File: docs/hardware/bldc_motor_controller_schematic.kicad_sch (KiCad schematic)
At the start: 17 parts, among them J1 J_NUCLEO_I2C, J10 J_DRV8313_CTRL, J11 J_AS5600, J12 J_INA226, J13 J_SSD1306, J14 J_BARREL_JACK1, J2 J_NUCLEO_PWM, J3 J_NUCLEO_GPIO, J4 J_NUCLEO_UART, J5 J_NUCLEO_PWR, J7 J_MOTOR, J8 J_HM10, J9 J_DRV8313_OUT

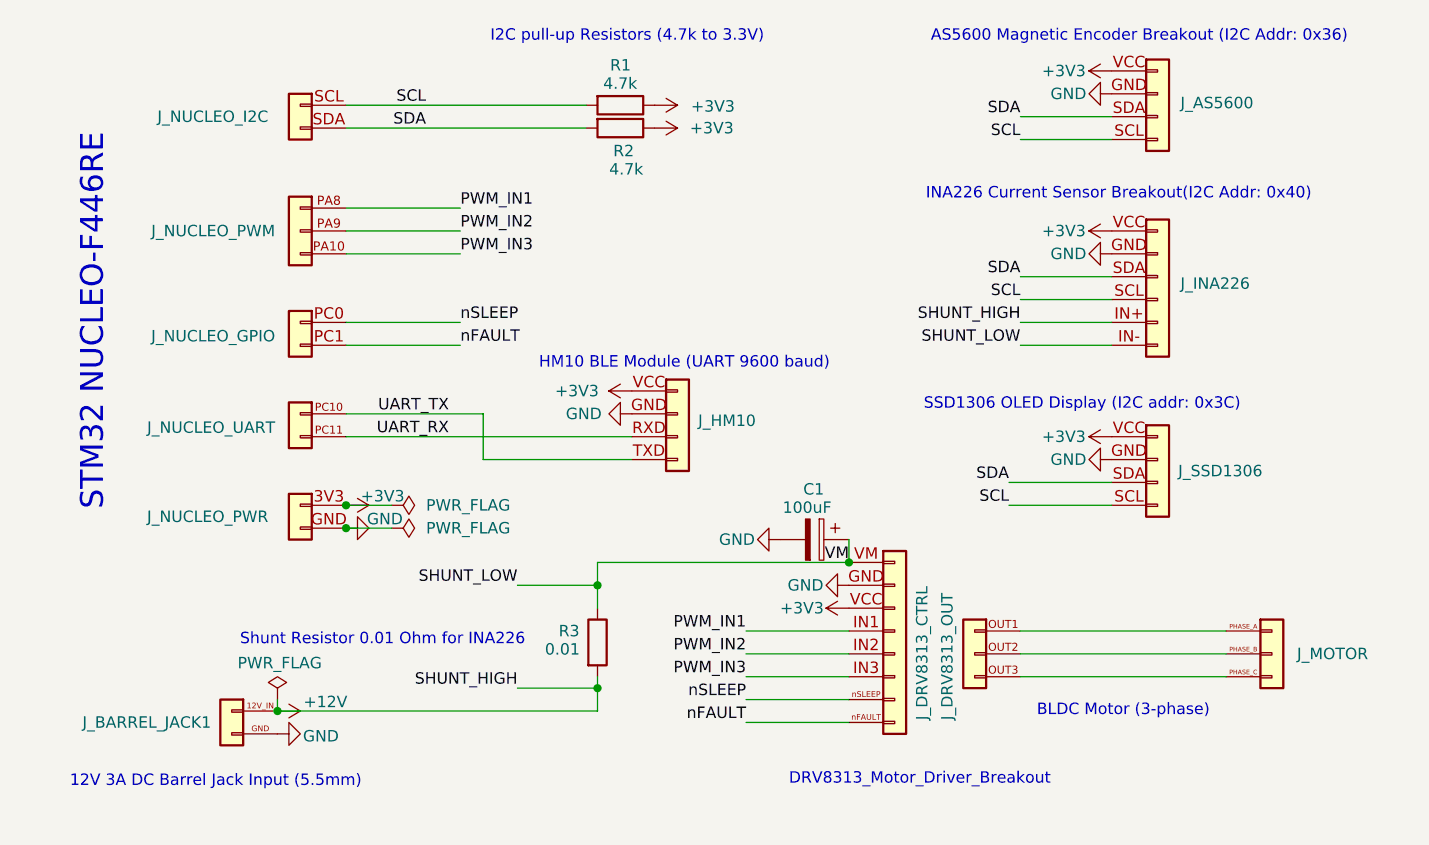
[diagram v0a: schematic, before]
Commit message: hw: update KiCad schematic files
- Remove on-board capacitor, pull-up resistors, and shunt resistor

- Add necessary pins to DRV8313 and INA226

- Fix UART to HM10 connections

- Add additional connections via net labels
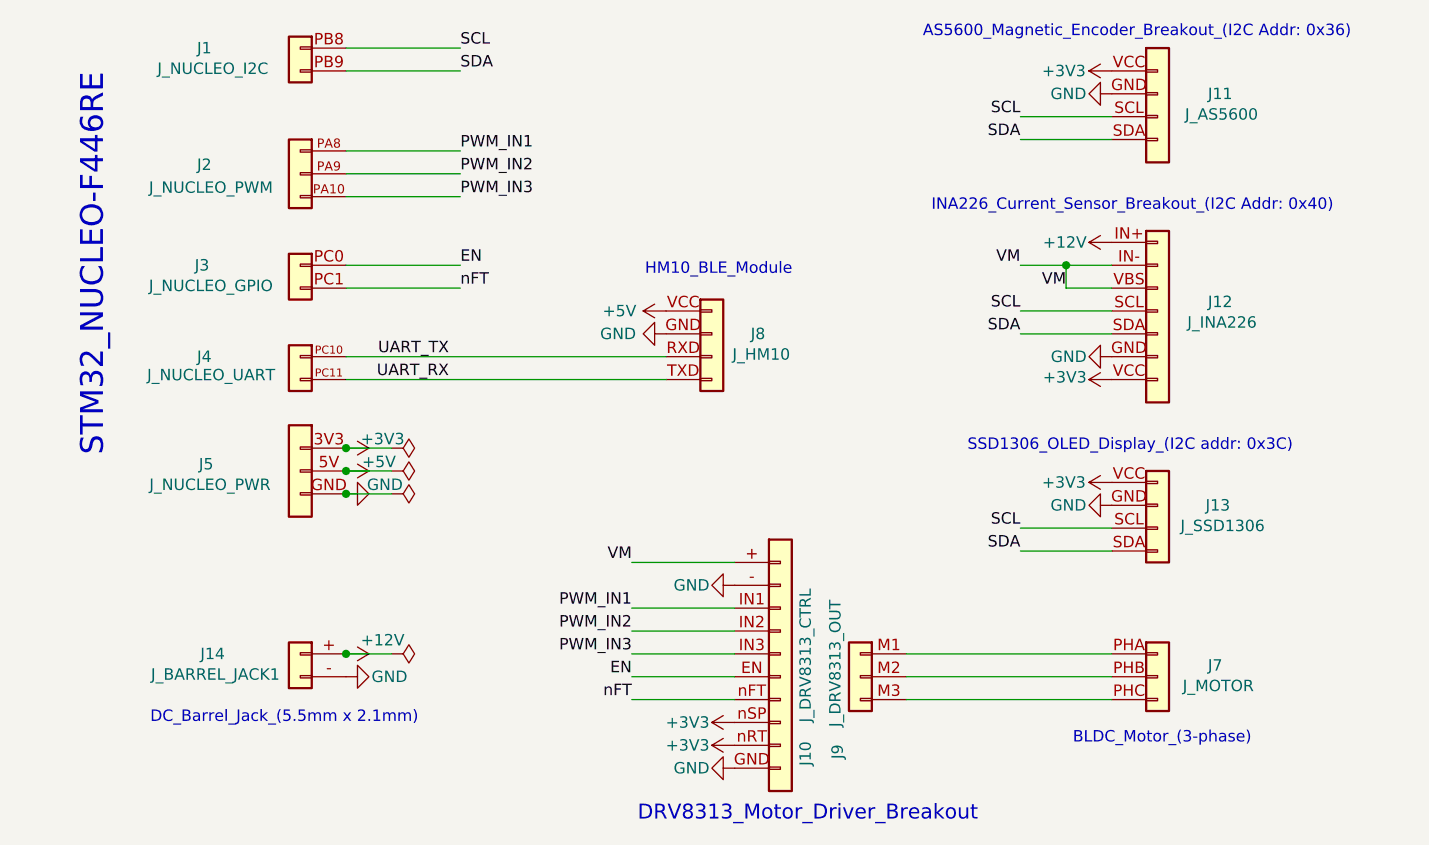
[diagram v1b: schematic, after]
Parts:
- removed C1: 100uF, symbol Device:C_Polarized
- removed R1, R2: 4.7k, symbol Device:R
- removed R3: 0.01, symbol Device:R
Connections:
- net +12V: now also J14.+; no longer J14.12V_IN
- net +3V3: now also J10.nRT, J10.nSP; no longer J10.VCC, J8.VCC
- net GND: now also J10.-, J14.-; no longer J14.GND
- net SCL: now also J1.PB8 (12V_IN); no longer J1.SCL (12V_IN)
- net SDA: now also J1.PB9 (GND); no longer J1.SDA (GND)
- net UART_RX: now also J8.TXD (SCL); no longer J8.RXD (SDA)
- net UART_TX: now also J8.RXD (SDA); no longer J8.TXD (SCL)
- net SHUNT_LOW renamed VM
- net VM: now also J10.+, J12.VBS; no longer J10.VM
- net nFAULT renamed nFT
- net nFT: now also J10.nFT; no longer J10.nFAULT
- net nSLEEP renamed EN
- net EN: now also J10.EN; no longer J10.nSLEEP
- new net: J7.PHA, J9.M1
- new net: J7.PHB, J9.M2
- new net: J7.PHC, J9.M3
- new net +5V: J5.5V, J8.VCC
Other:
- note added: "AS5600_Magnetic_Encoder_Breakout_(I2C Addr: 0x36)"
- note added: "BLDC_Motor_(3-phase)"
- note added: "DC_Barrel_Jack_(5.5mm x 2.1mm)"
- note added: "HM10_BLE_Module"
- note added: "INA226_Current_Sensor_Breakout_(I2C Addr: 0x40)"
- note added: "SSD1306_OLED_Display_(I2C addr: 0x3C)"
- note added: "STM32_NUCLEO-F446RE"
- note removed: "12V 3A DC Barrel Jack Input (5.5mm)"
- note removed: "AS5600 Magnetic Encoder Breakout (I2C Addr: 0x36)"
- note removed: "BLDC Motor (3-phase)"
- note removed: "HM10 BLE Module (UART 9600 baud)"
- note removed: "I2C pull-up Resistors (4.7k to 3.3V)"
- note removed: "INA226 Current Sensor Breakout(I2C Addr: 0x40)"
- note removed: "SSD1306 OLED Display (I2C addr: 0x3C)"
- note removed: "STM32 NUCLEO-F446RE"
- note removed: "Shunt Resistor 0.01 Ohm for INA226"
